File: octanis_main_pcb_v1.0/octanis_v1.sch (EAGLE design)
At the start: 107 parts, among them IC1 BNO055A, IC2 BME280, Q1 32.768kHz, Q2 32.768kHz, U1 TPS61232, U10 INA210, U100 RN2483, U11 DRV8836DSSR, U12 DRV8836DSSR, U2 MSP432, U3 MAX6001SOT-23, U4 DRV8836DSSR, U5 DRV8836DSSR, U6 SST25VF064C, U7 INA210, U8 INA210, U9 INA210

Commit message: started v1.0 mainboard
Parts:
- removed 5V: 5V-ok, adafruit:LEDCHIPLED_0603
- removed C10: 10nF, rcl:C-EUC0603
- removed JP1: (no value), pinhead-2:PINHD-2X05_2.54
- removed LED33_J: (no value), jumper:SJ
- removed U1: TPS61232, texasinstruments:TPS61232
- added BAT: BAT-ok, adafruit:LEDCHIPLED_0603
- added C36, C37: 470n, rcl:C-EUC0603
- added IC3: TPS61201, texas:TPS61201
- added JP4: (no value), pinhead-2:PINHD-2X06_2.54-SMD
- added TP1, TP2: TPTP06R, testpad:TPTP06R
- C1, C7, C8: value 22uF -> 10u; device rcl:C-EUC0603 -> rcl:C-EUC0805K
- C9: value 3 x 22uF -> 100n
- JP2: device pinhead-2:PINHD-2X05_2.54-SMD -> pinhead-2:PINHD-2X04_2.54
- L1: value 1uH -> LPS3015; device Coilcraft:XFL4020 -> inductor-coilcraft:LPS3015
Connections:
- removed net IND: L1.2, U1.SW
- removed net N$14: LED5_J.2, R6.1
- removed net P7.5: DIGITAL_IO2.10, U2.P7.5/PM_TA1.3/C0.4
- removed net P7.6: DIGITAL_IO2.9, U2.P7.6/PM_TA1.2/C0.3
- new net L: IC3.L, L1.2
- new net N$20: TP2.TP, U5.MODE
- new net N$22: TP1.TP, U4.MODE
- new net P8.0: DIGITAL_IO2.10, U2.P8.0/UCB3STE/TA1.0/C0.1
- new net P8.1: DIGITAL_IO2.9, U2.P8.1/UCB3CLK/TA2.0/C0.0
- net +3V3: now also C7.1, C8.1, IC3.VOUT, JP4.10, JP4.3, JP4.9; no longer JP2.10, JP2.3, JP2.9
- net +5V: now also JP2.7, JP2.8; no longer 5V.A, C7.1, C8.1, C9.1, JP1.10, JP1.9, R7.2, U1.FB, U1.VOUT
- net 3V3_MODULE2: now also BAT.A, IC3.EN, IC3.PS, IC3.VIN, JP2.3, JP2.4; no longer JP1.5, JP1.6, U1.VIN
- net 5VEN: no longer R1.1, U1.EN
- net EXT_LIGHTNING_INT: now also JP4.2; no longer JP2.2
- net EXT_UV_EN: now also JP4.1; no longer JP2.1
- net GND: now also C36.2, C37.2, IC3.GND, IC3.PGND, IC3.PP, IC3.PP@1, IC3.PP@2, JP2.1, JP2.2, JP2.5, JP2.6, JP4.11, JP4.12, JP4.4, R7.1; no longer C10.2, JP1.1, JP1.2, JP1.3, JP1.4, JP1.7, JP1.8, JP2.4, LED33_J.1, U1.GND, U1.GND1, U1.GND2, U1.GND3, U1.GND4, U1.GND5
- net M5678SLEEP: now also C36.1, C37.1; no longer U4.MODE, U5.MODE
- net M5IN1: now also U2.P7.5/PM_TA1.3/C0.4; no longer U2.P7.7/PM_TA1.1/C0.2
- net M5IN2: now also U2.P7.6/PM_TA1.2/C0.3; no longer U2.P8.0/UCB3STE/TA1.0/C0.1
- net M6IN1: now also U2.P7.7/PM_TA1.1/C0.2; no longer U2.P3.0/PM_UCA2STE
- net M6IN2: now also U2.P3.0/PM_UCA2STE; no longer U2.P8.1/UCB3CLK/TA2.0/C0.0
- net N$2: now also C9.1, IC3.VAUX; no longer R7.1, U1.PG
- net N$26: now also LED5_J.2, R6.1; no longer LED33_J.2
- net N$42: now also IC3.UVLO, R1.1, R7.2; no longer C10.1, U1.SS
- net N$44: now also BAT.C; no longer 5V.C
- net SCL: now also JP4.5, JP4.7; no longer JP2.5, JP2.7
- net SDA: now also JP4.6, JP4.8; no longer JP2.6, JP2.8
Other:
- moved on the sheet: 3V, C7, C8, C9, LED5_J, R1, R6, R7, R8

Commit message: added 5V on-off switch and battery boost converter to mainboard
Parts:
- removed R1: 1M, rcl:R-EU_R0603
- added 5VEXT: (no value), Headerlibrary:PINHD-1X1
- added R101: 2k, rcl:R-EU_R0603
- added R102: 1k, rcl:R-EU_R0603
- added T1, T3, T4: (no value), zetex:NMOSSOT23
- added T2: (no value), zetex:PMOSSOT23
- C7: value 10u -> 100n; device rcl:C-EUC0805K -> rcl:C-EUC0603
- C9: value 100n -> 10u; device rcl:C-EUC0603 -> rcl:C-EUC0805K
- R6: value 2k -> 1M
- R8: value 1k -> 1M
- renumbered TP1 to MOD., TP2 to MOD
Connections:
- removed net 5VEN: U2.P2.0/PM_UCA1STE
- new net 5V_EN: T1.G, U2.P2.0/PM_UCA1STE
- new net N$14: R8.1, T1.D, T2.G
- new net N$46: DIGITAL_IO1.9, T3.D
- new net N$47: 5VEXT.1, T2.S
- new net N$55: DIGITAL_IO1.10, T4.D
- net +3V3: now also C9.1; no longer C7.1
- net +5V: now also R8.2, T2.D
- net 3V3_MODULE2: now also R6.2; no longer R1.2
- net GND: now also T1.S, T3.S, T4.S
- net N$2: now also C7.1; no longer C9.1
- net N$26: now also R101.1, R102.1; no longer R6.1, R8.1
- net N$4: now also R102.2; no longer R8.2
- net N$42: now also R6.1; no longer R1.1
- net N$44: now also R101.2; no longer R6.2
- net PJ.2: now also T4.G; no longer DIGITAL_IO1.10
- net PJ.3: now also T3.G; no longer DIGITAL_IO1.9
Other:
- moved on the sheet: C7, C8, C9, R6, R8

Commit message: silkscreen artwork, lightning input interrupt
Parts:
- removed C35: 120n, rcl:C-EUC0603
- added C10: 10u, rcl:C-EUC0805K
- added U$3: BNO055_COORDINATES, Octanis1:BNO055_COORDINATES
- added VCCMOT: TPTP06R, testpad:TPTP06R
- C21, C22: value 100n -> 470n
- C28: value 470n -> 10n
- C30: value 10n -> 470n
- C36, C37: value 470n -> 100n
- C5: value 12p -> 120n
- C7: value 100n -> 12p
- C8: value 10u -> 100n; device rcl:C-EUC0805K -> rcl:C-EUC0603
- LORA_RST_N: value (none) -> PTR1TP15R; device Headerlibrary:PINHD-1X1 -> testpad:PTR1TP15R
- renumbered IC3 to U1
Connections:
- removed net P9.4: DIGITAL_IO1.18, U2.P9.4/UCA3STE
- net +3V3: now also C10.1, C36.2, C37.1, C5.1; no longer C21.2, C22.1, C35.1, C8.1
- net A20: now also C29.2; no longer C32.2
- net A21: now also C32.2; no longer C31.2
- net A22: now also C31.2; no longer C28.2
- net A23: now also C30.2; no longer C29.2
- net CURR_SENSE_EN: now also C28.2; no longer C30.2
- net GND: now also C10.2, C21.2, C36.1, DIGITAL_IO1.18; no longer C21.1, C35.2, C36.2
- net LORA_RST_N: now also LORA_RST_N.TP, U2.P9.4/UCA3STE; no longer LORA_RST_N.1
- net M5678SLEEP: now also C21.1, C22.1, VCCMOT.TP; no longer C36.1, C37.1
- net N$19: now also C6.1; no longer C5.1
- net N$2: now also C8.1; no longer C7.1
- net N$73: now also C7.1; no longer C6.1
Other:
- moved on the sheet: C21, C22, C28, C29, C30, C31, C32, C36, C37, C5, C6, C7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

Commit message: octanis 1.0 finished
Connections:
- net 5V_EN: now also U2.P1.4/UCB0STE; no longer U2.P2.0/PM_UCA1STE
- net EXT_LIGHTNING_INT: now also U2.P2.0/PM_UCA1STE; no longer U2.P1.4/UCB0STE
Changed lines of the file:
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@@
 <net name="EXT_LIGHTNING_INT" class="0">
-<segment>
-<pinref part="U2" gate="MSP432" pin="P1.4/UCB0STE"/>
-<wire x1="287.02" y1="327.66" x2="271.78" y2="327.66" width="0.1524" layer="91"/>
-<label x="271.78" y="327.66" size="1.27" layer="95"/>
-<label x="271.78" y="327.66" size="1.27" layer="95"/>
-</segment>
 <segment>
 <wire x1="236.22" y1="459.74" x2="241.3" y2="459.74" width="0.1524" layer="91"/>
@@
 <pinref part="JP4" gate="A" pin="2"/>
 <junction x="231.14" y="459.74"/>
+</segment>
+<segment>
+<pinref part="U2" gate="MSP432" pin="P2.0/PM_UCA1STE"/>
+<wire x1="287.02" y1="314.96" x2="276.86" y2="314.96" width="0.1524" layer="91"/>
+<wire x1="276.86" y1="314.96" x2="274.32" y2="314.96" width="0.1524" layer="91"/>
+<label x="274.32" y="314.96" size="1.27" layer="95" rot="R180" xref="yes"/>
 </segment>
 </net>
@@
 </segment>
 <segment>
-<pinref part="U2" gate="MSP432" pin="P2.0/PM_UCA1STE"/>
-<wire x1="287.02" y1="314.96" x2="276.86" y2="314.96" width="0.1524" layer="91"/>
-<wire x1="276.86" y1="314.96" x2="274.32" y2="314.96" width="0.1524" layer="91"/>
-<label x="274.32" y="314.96" size="1.27" layer="95" rot="R180" xref="yes"/>
-</segment>
-</net>
+<pinref part="U2" gate="MSP432" pin="P1.4/UCB0STE"/>
+<wire x1="287.02" y1="327.66" x2="271.78" y2="327.66" width="0.1524" layer="91"/>
+<label x="271.78" y="327.66" size="1.27" layer="95"/>
+<label x="271.78" y="327.66" size="1.27" layer="95"/>
+</segment>
+</net>

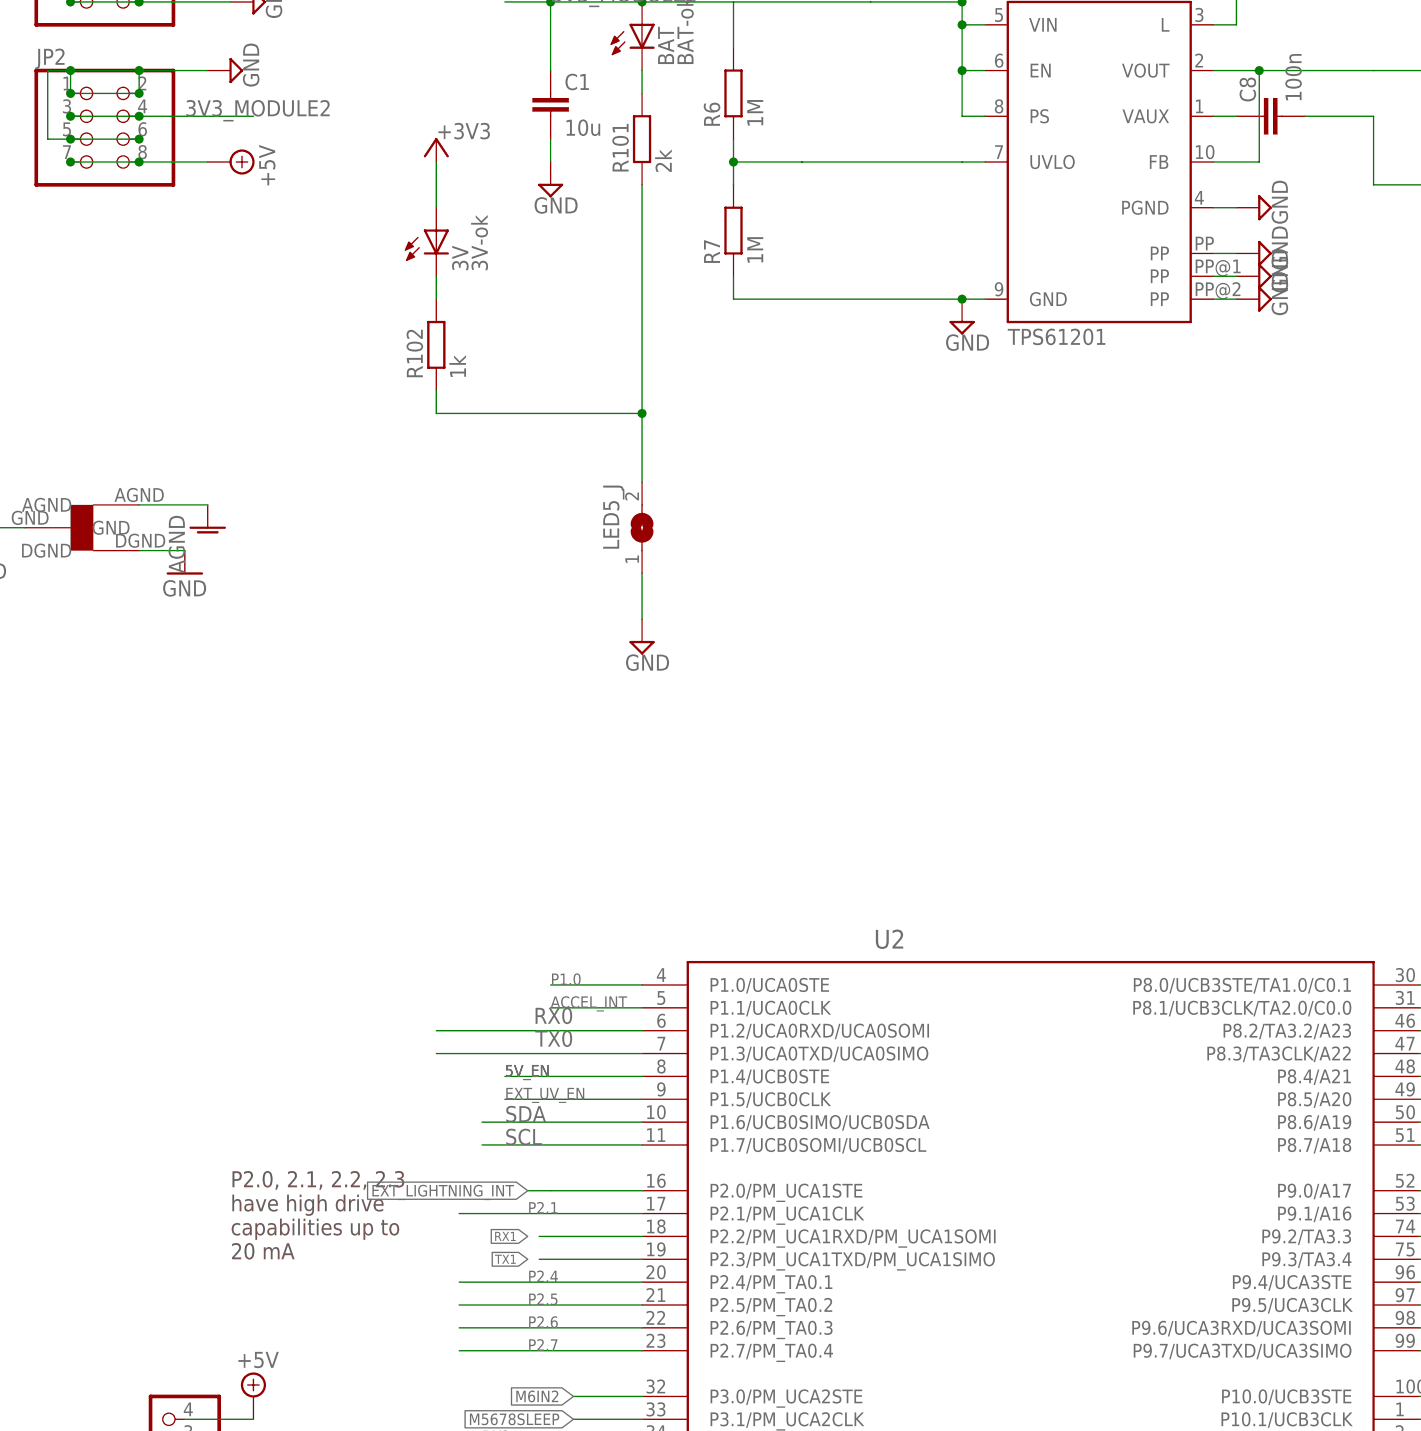
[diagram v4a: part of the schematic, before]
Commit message: corrected the feedback pin error on battery DC-DC converter.
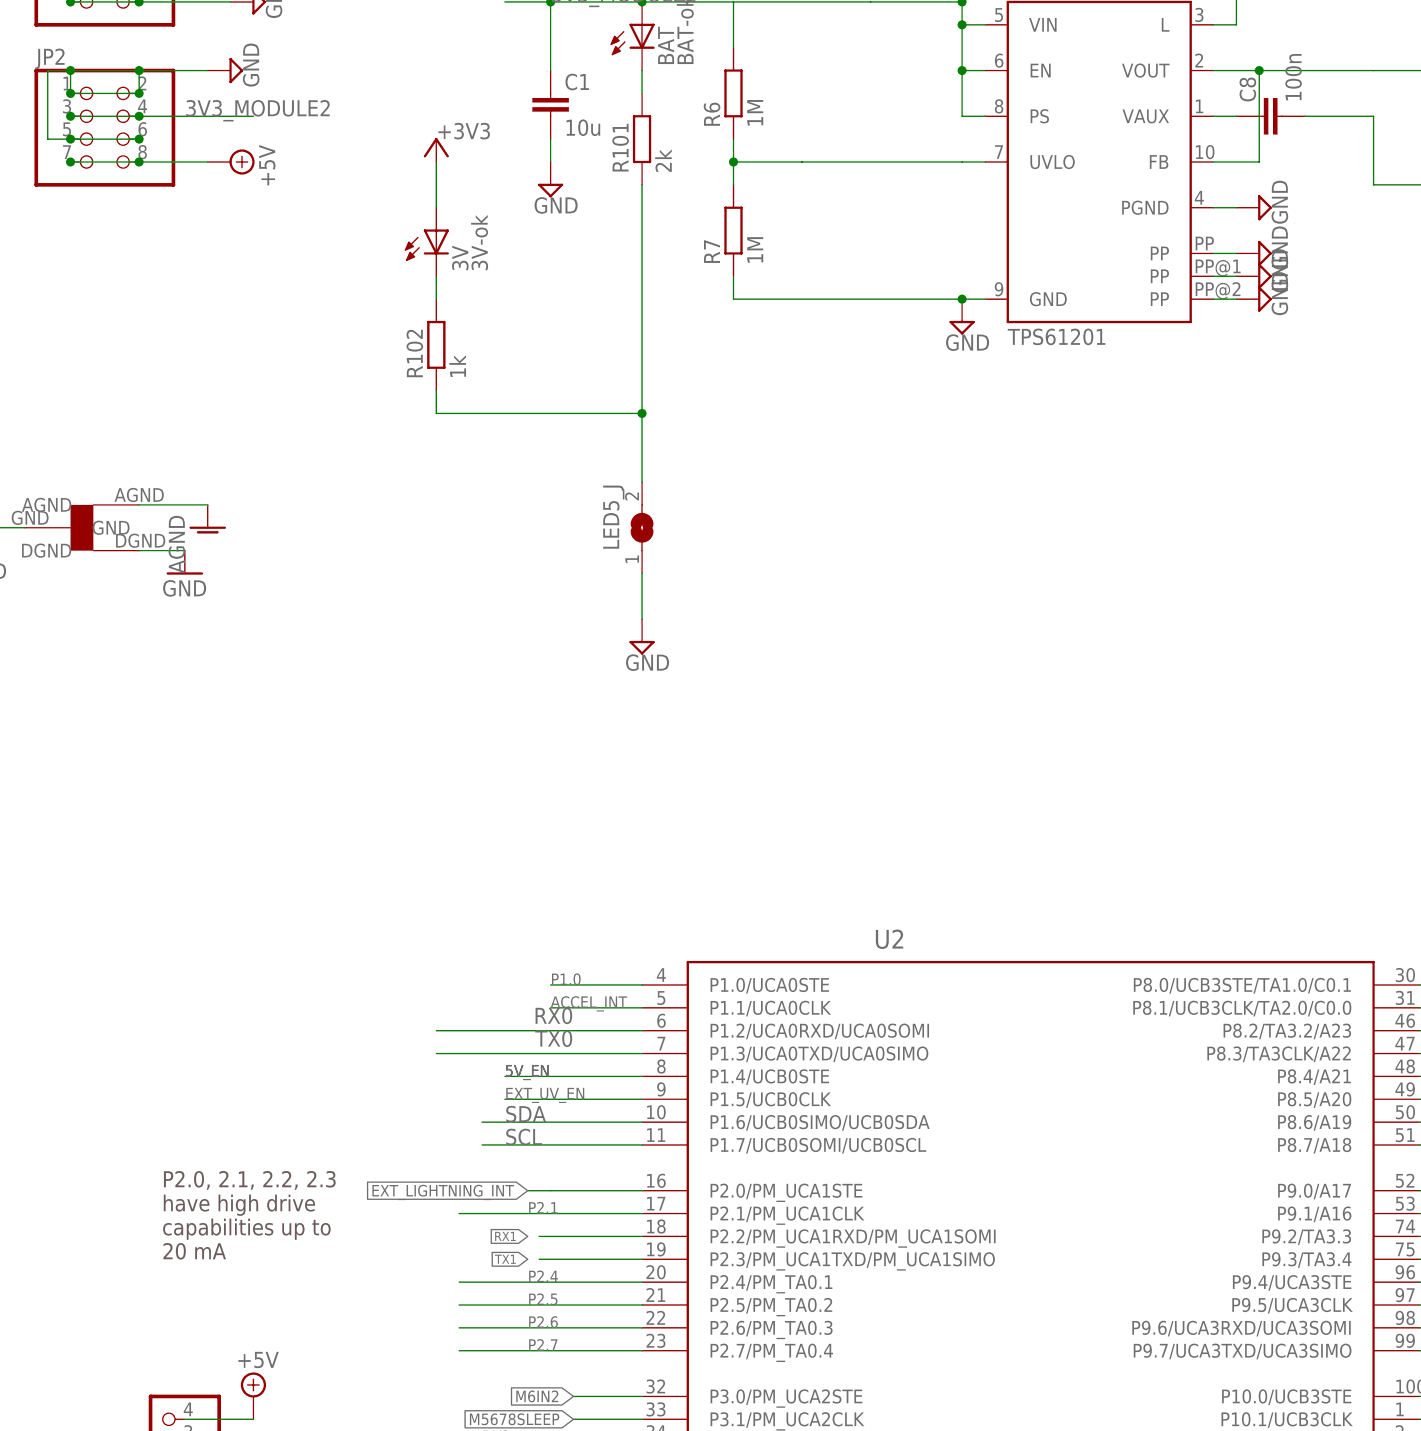
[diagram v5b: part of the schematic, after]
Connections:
- net +3V3: now also U1.FB
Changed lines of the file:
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@@
 <wire x1="440.69" y1="193.04" x2="440.69" y2="148.59" width="0.1524" layer="95" style="shortdash"/>
 <wire x1="440.69" y1="148.59" x2="421.64" y2="148.59" width="0.1524" layer="95" style="shortdash"/>
-<text x="241.3" y="307.34" size="1.778" layer="97">P2.0, 2.1, 2.2, 2.3
+<text x="233.68" y="307.34" size="1.778" layer="97">P2.0, 2.1, 2.2, 2.3
 have high drive
 capabilities up to
@@
 <wire x1="406.4" y1="439.42" x2="419.1" y2="439.42" width="0.1524" layer="91"/>
 <label x="416.56" y="436.88" size="1.778" layer="95"/>
-<wire x1="350.52" y1="429.26" x2="355.6" y2="429.26" width="0.1524" layer="91"/>
 <wire x1="355.6" y1="429.26" x2="355.6" y2="439.42" width="0.1524" layer="91"/>
 <pinref part="+3V12" gate="G$1" pin="+3V3"/>
@@
 <wire x1="350.52" y1="439.42" x2="355.6" y2="439.42" width="0.1524" layer="91"/>
 <junction x="355.6" y="439.42"/>
+<pinref part="U1" gate="G$1" pin="FB"/>
+<wire x1="355.6" y1="429.26" x2="350.52" y2="429.26" width="0.1524" layer="91"/>
 </segment>
 </net>
